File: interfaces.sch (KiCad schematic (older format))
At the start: 69 parts, among them IC3 TPD8S009DSMR, J4 WE_629105150521, J6 685119134923, J7 1140084168, Q2 BSS138APW, Q3 BSS138APW, Q4 BSS138APW, Q5 BSS138APW, Q6 BSS138APW, U12 FT2232HQ

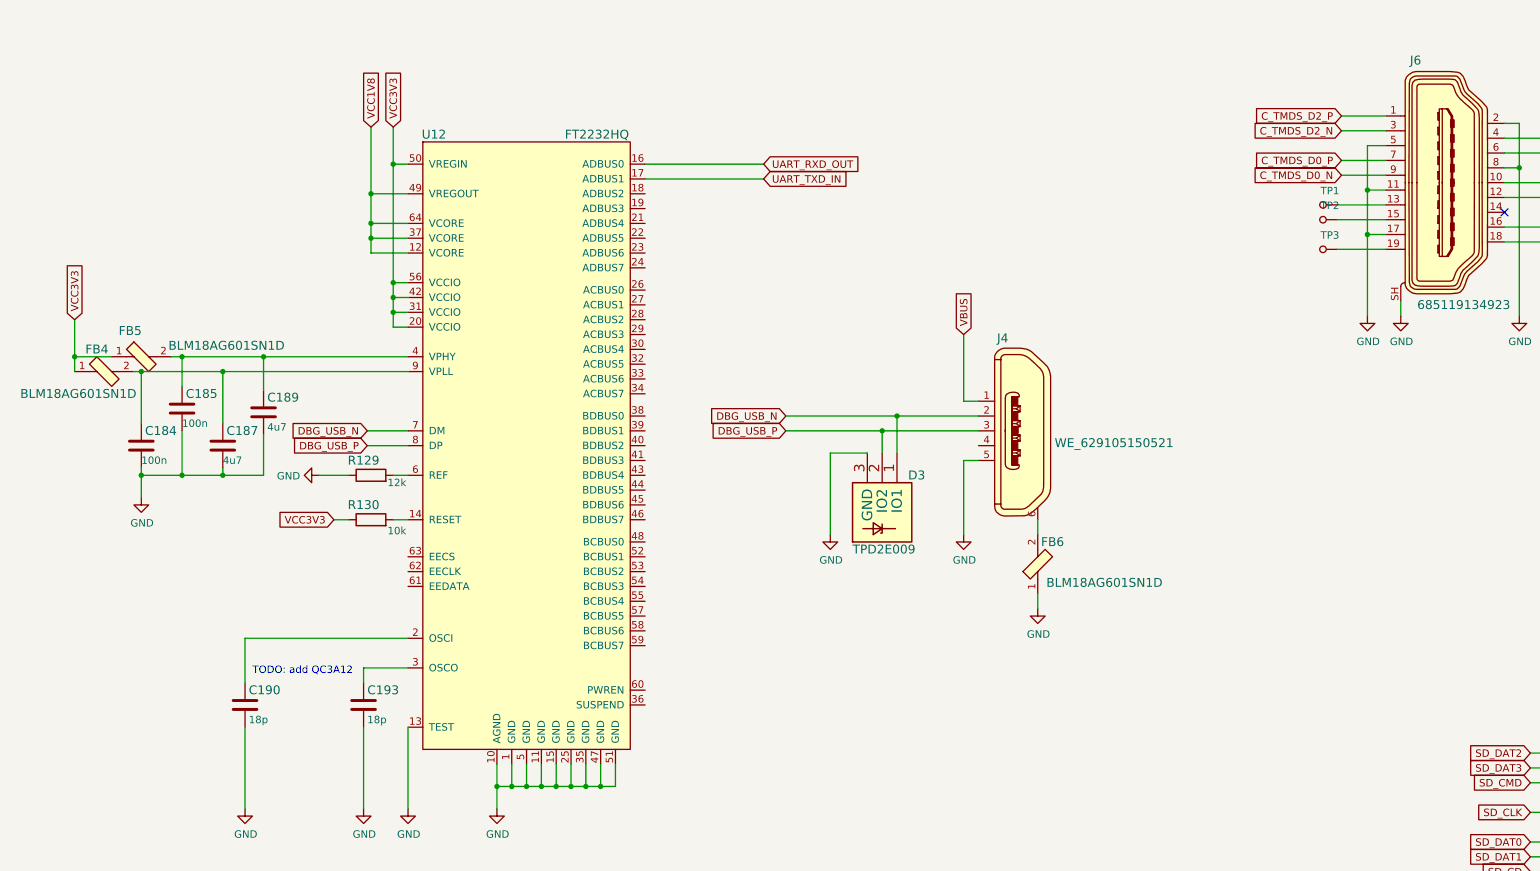
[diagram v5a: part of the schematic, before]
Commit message: Introduce FT4232HQ
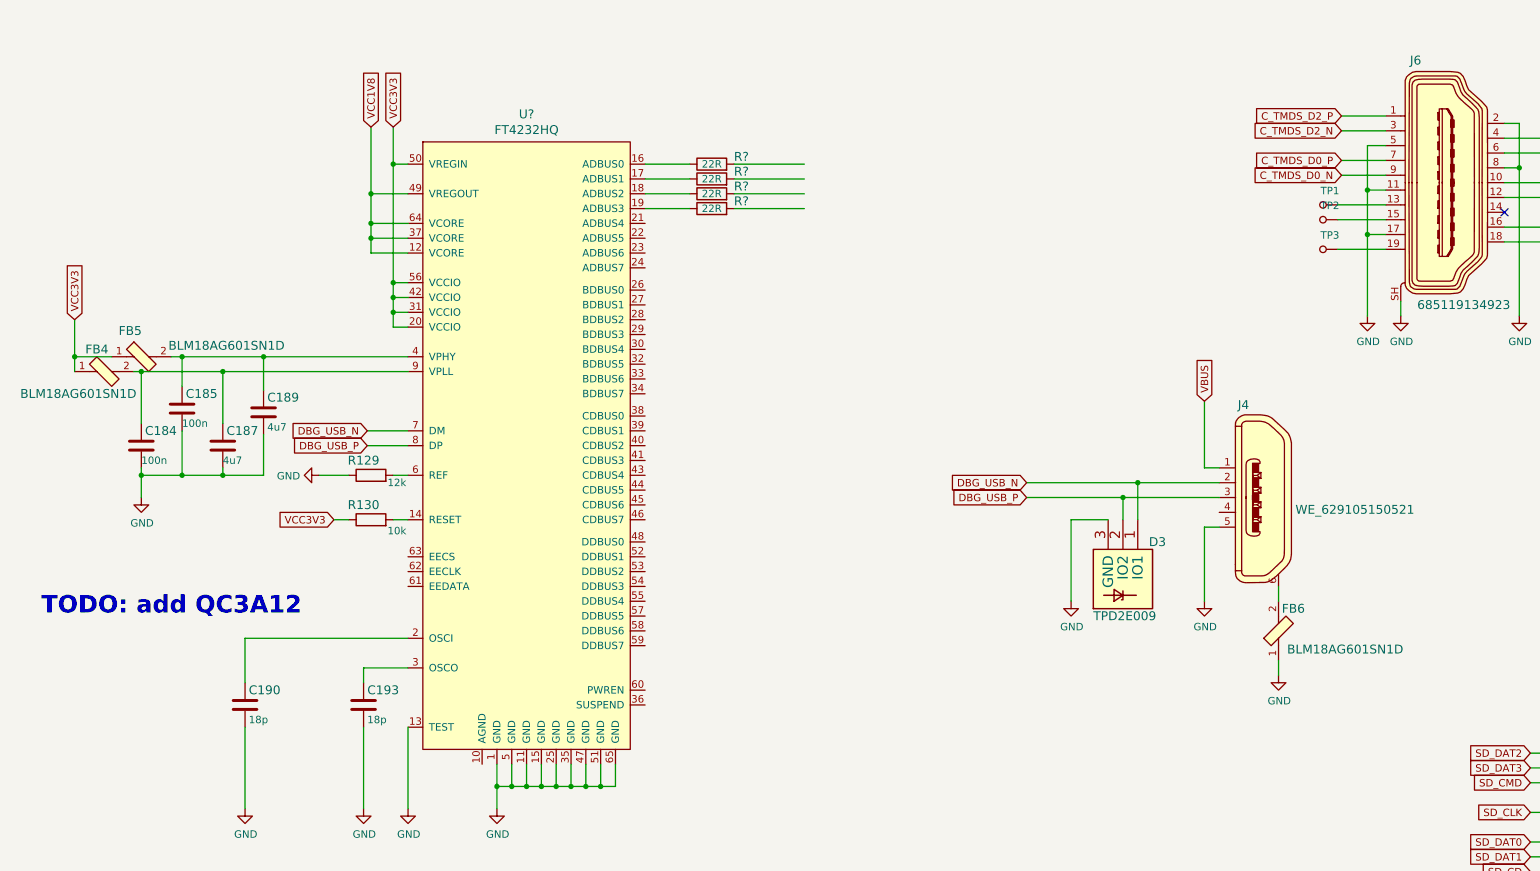
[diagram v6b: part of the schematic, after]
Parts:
- removed U12: FT2232HQ, lpddr4-test-board-footprints:QFN50P900X900X100-65N, symbol lpddr4-test-board:FT2232HQ
- added R? (x4): R_22R_0402, antmicro-footprints:0402-res, symbol antmicroResistors0402:R_22R_0402
- added U?: FT4232HQ, antmicro-footprints:FT4232HQ, symbol antmicroInterfaceControllers:FT4232HQ
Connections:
- net DBG_USB_N: now also U?.7 (DM)
- net DBG_USB_P: now also U?.8 (DP)
- net GND: now also U?.1 (GND), U?.11 (GND), U?.13 (TEST), U?.15 (GND), U?.25 (GND), U?.35 (GND), U?.47 (GND), U?.5 (GND), U?.51 (GND), U?.65 (GND)
- net VCC1V8: now also U?.12 (VCORE), U?.37 (VCORE), U?.49 (VREGOUT), U?.64 (VCORE)
- net VCC3V3: now also U?.20 (VCCIO), U?.31 (VCCIO), U?.42 (VCCIO), U?.50 (VREGIN), U?.56 (VCCIO)
- net at C185.1, C189.1, FB5.2: now also U?.4 (VPHY)
- net at C184.1, C187.1, FB4.2: now also U?.9 (VPLL)
- net at R129.2: now also U?.6 (REF)
- net at R130.2: now also U?.14 (RESET)
- net at C190.1: now also U?.2 (OSCI)
- net at C193.1: now also U?.3 (OSCO)
- new net: R?.1, U?.16 (ADBUS0)
- new net: R?.1, U?.17 (ADBUS1)
- new net: R?.1, U?.18 (ADBUS2)
- new net: R?.1, U?.19 (ADBUS3)
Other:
- moved on the sheet: D3, FB6, J4
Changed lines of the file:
@@
 Comment4 ""
 $EndDescr
-Text GLabel 5950 3000 2    50   Input ~ 0
-UART_RXD_OUT
-Text GLabel 5950 3100 2    50   Input ~ 0
-UART_TXD_IN
-Wire Wire Line
-	5150 3000 5950 3000
-Wire Wire Line
-	5150 3100 5950 3100
 Wire Wire Line
 	3550 3000 3450 3000
@@
 Wire Wire Line
 	3150 5400 3050 5400
-Text Notes 2500 6450 0    50   ~ 0
+Text Notes 1075 6050 0    118  ~ 24
 TODO: add QC3A12
 Wire Wire Line
@@
 	1    0    0    -1
 $EndComp
-$Comp
-L lpddr4-test-board:FT2232HQ U12
-U 1 1 600E77E5
-P 4350 5150
-F 0 "U12" H 3725 7500 60  0000 C CNN
-F 1 "FT2232HQ" H 4825 7500 60  0000 C CNN
-F 2 "lpddr4-test-board-footprints:QFN50P900X900X100-65N" V 4550 5350 60  0001 L CNN
-F 3 "https://www.ftdichip.com/Support/Documents/DataSheets/ICs/DS_FT2232H.pdf" H 4550 5550 60  0001 L CNN
-F 4 "FTDI" H 4550 6300 60  0001 L CNN "Manufacturer"
-F 5 "FT2232HQ-TRAY" H 4550 5700 60  0001 L CNN "MPN"
-	1    4350 5150
-	1    0    0    -1
-$EndComp
 Wire Wire Line
 	4150 7050 4150 7200
@@
 L lpddr4-test-board:WE_629105150521 J4
 U 1 1 60021F87
-P 7700 4800
-F 0 "J4" H 7875 5425 60  0000 R CNN
-F 1 "WE_629105150521" H 7486 4718 60  0000 R CNN
-F 2 "lpddr4-test-board-footprints:USB_Micro_B_Female_629105150521" H 7900 5000 60  0001 L CNN
-F 3 "" H 7900 5100 60  0001 L CNN
-F 4 "629105150521" H 7900 5300 60  0001 L CNN "MPN"
-F 5 "Wurth_Elektronik" H 7900 5900 60  0001 L CNN "Manufacturer"
-	1    7700 4800
+P 9325 5250
+F 0 "J4" H 9500 5875 60  0000 R CNN
+F 1 "WE_629105150521" H 9111 5168 60  0000 R CNN
+F 2 "lpddr4-test-board-footprints:USB_Micro_B_Female_629105150521" H 9525 5450 60  0001 L CNN
+F 3 "" H 9525 5550 60  0001 L CNN
+F 4 "629105150521" H 9525 5750 60  0001 L CNN "MPN"
+F 5 "Wurth_Elektronik" H 9525 6350 60  0001 L CNN "Manufacturer"
+	1    9325 5250
 	-1   0    0    -1
 $EndComp
 Wire Wire Line
-	7400 5000 7300 5000
-Wire Wire Line
-	7300 5000 7300 5500
+	9025 5450 8925 5450
+Wire Wire Line
+	8925 5450 8925 5950
 $Comp
 L lpddr4-test-board:GND #PWR0226
 U 1 1 6002BAB6
-P 7300 5500
-F 0 "#PWR0226" H 7300 5250 50  0001 C CNN
-F 1 "GND" H 7305 5327 50  0000 C CNN
-F 2 "" H 7300 5500 50  0001 C CNN
-F 3 "" H 7300 5500 50  0001 C CNN
-	1    7300 5500
+P 8925 5950
+F 0 "#PWR0226" H 8925 5700 50  0001 C CNN
+F 1 "GND" H 8930 5777 50  0000 C CNN
+F 2 "" H 8925 5950 50  0001 C CNN
+F 3 "" H 8925 5950 50  0001 C CNN
+	1    8925 5950
 	1    0    0    -1
 $EndComp
@@
 L lpddr4-test-board:BLM18AG601SN1D FB6
 U 1 1 6002DC37
-P 7800 5700
-F 0 "FB6" V 7950 5600 60  0000 C CNN
-F 1 "BLM18AG601SN1D" V 7675 5250 60  0000 C CNN
-F 2 "lpddr4-test-board-footprints:0603" H 8000 5900 60  0001 L CNN
-F 3 "https://www.murata.com/en-us/products/productdata/8796738650142/ENFA0003.pdf" H 8000 6000 60  0001 L CNN
-F 4 "BLM18AG601SN1D" H 8000 6200 60  0001 L CNN "MPN"
-F 5 "Murata Electronics North America" H 8000 6800 60  0001 L CNN "Manufacturer"
-	1    7800 5700
+P 9425 6150
+F 0 "FB6" V 9575 6050 60  0000 C CNN
+F 1 "BLM18AG601SN1D" V 9300 5700 60  0000 C CNN
+F 2 "lpddr4-test-board-footprints:0603" H 9625 6350 60  0001 L CNN
+F 3 "https://www.murata.com/en-us/products/productdata/8796738650142/ENFA0003.pdf" H 9625 6450 60  0001 L CNN
+F 4 "BLM18AG601SN1D" H 9625 6650 60  0001 L CNN "MPN"
+F 5 "Murata Electronics North America" H 9625 7250 60  0001 L CNN "Manufacturer"
+	1    9425 6150
 	0    -1   -1   0
 $EndComp
-Text GLabel 6100 4700 0    50   Input ~ 0
+Text GLabel 7725 5150 0    50   Input ~ 0
 DBG_USB_N
-Text GLabel 6100 4800 0    50   Input ~ 0
+Text GLabel 7725 5250 0    50   Input ~ 0
 DBG_USB_P
 Wire Wire Line
-	7400 4600 7300 4600
-Wire Wire Line
-	7300 4600 7300 4150
+	9025 5050 8925 5050
+Wire Wire Line
+	8925 5050 8925 4600
 Text GLabel 2350 8375 1    50   Input ~ 0
 VCC3V3
@@
 L lpddr4-test-board:TPD2E009 D3
 U 1 1 6003C213
-P 6850 5150
-F 0 "D3" V 6800 5225 60  0000 L CNN
-F 1 "TPD2E009" V 7300 4850 60  0000 L CNN
-F 2 "lpddr4-test-board-footprints:SOT-3" H 6900 5350 60  0001 C CNN
-F 3 "https://www.ti.com/lit/ds/symlink/tpd2e009.pdf?ts=1597910439511&ref_url=https%253A%252F%252Fwww.google.com%252F" H 6850 5150 60  0001 C CNN
-F 4 "TPD2E009DRTR" H 6550 5450 50  0001 C CNN "MPN"
-F 5 "Texas Instruments" H 6550 5550 50  0001 C CNN "Manufacturer"
-	1    6850 5150
-	0    1    1    0
-$EndComp
-Wire Wire Line
-	6100 4700 6850 4700
-Wire Wire Line
-	6100 4800 6750 4800
-Wire Wire Line
-	6850 4950 6850 4700
-Connection ~ 6850 4700
-Wire Wire Line
-	6850 4700 7400 4700
-Wire Wire Line
-	6750 4950 6750 4800
-Connection ~ 6750 4800
-Wire Wire Line
-	6750 4800 7400 4800
-Wire Wire Line
-	6650 4950 6400 4950
-Wire Wire Line
-	6400 4950 6400 5500
+P 8475 5600
+F 0 "D3" V 8425 5675 60  0000 L CNN
+F 1 "TPD2E009" V 8925 5300 60  0000 L CNN
+F 2 "lpddr4-test-board-footprints:SOT-3" H 8525 5800 60  0001 C CNN
+F 3 "https://www.ti.com/lit/ds/symlink/tpd2e009.pdf?ts=1597910439511&ref_url=https%253A%252F%252Fwww.google.com%252F" H 8475 5600 60  0001 C CNN
+F 4 "TPD2E009DRTR" H 8175 5900 50  0001 C CNN "MPN"
+F 5 "Texas Instruments" H 8175 6000 50  0001 C CNN "Manufacturer"
+	1    8475 5600
+	0    1    1    0
+$EndComp
+Wire Wire Line
+	7725 5150 8475 5150
+Wire Wire Line
+	7725 5250 8375 5250
+Wire Wire Line
+	8475 5400 8475 5150
+Connection ~ 8475 5150
+Wire Wire Line
+	8475 5150 9025 5150
+Wire Wire Line
+	8375 5400 8375 5250
+Connection ~ 8375 5250
+Wire Wire Line
+	8375 5250 9025 5250
+Wire Wire Line
+	8275 5400 8025 5400
+Wire Wire Line
+	8025 5400 8025 5950
 $Comp
 L lpddr4-test-board:GND #PWR0228
 U 1 1 60049482
-P 6400 5500
-F 0 "#PWR0228" H 6400 5250 50  0001 C CNN
-F 1 "GND" H 6405 5327 50  0000 C CNN
-F 2 "" H 6400 5500 50  0001 C CNN
-F 3 "" H 6400 5500 50  0001 C CNN
-	1    6400 5500
+P 8025 5950
+F 0 "#PWR0228" H 8025 5700 50  0001 C CNN
+F 1 "GND" H 8030 5777 50  0000 C CNN
+F 2 "" H 8025 5950 50  0001 C CNN
+F 3 "" H 8025 5950 50  0001 C CNN
+	1    8025 5950
 	1    0    0    -1
 $EndComp
@@
 Text GLabel 3050 5400 0    50   Input ~ 0
 VCC3V3
-Text GLabel 7300 4150 1    50   Input ~ 0
+Text GLabel 8925 4600 1    50   Input ~ 0
 VBUS
 $Comp
@@
 L lpddr4-test-board:GND #PWR0227
 U 1 1 6002DF17
-P 7800 6000
-F 0 "#PWR0227" H 7800 5750 50  0001 C CNN
-F 1 "GND" H 7805 5827 50  0000 C CNN
-F 2 "" H 7800 6000 50  0001 C CNN
-F 3 "" H 7800 6000 50  0001 C CNN
-	1    7800 6000
+P 9425 6450
+F 0 "#PWR0227" H 9425 6200 50  0001 C CNN
+F 1 "GND" H 9430 6277 50  0000 C CNN
+F 2 "" H 9425 6450 50  0001 C CNN
+F 3 "" H 9425 6450 50  0001 C CNN
+	1    9425 6450
 	1    0    0    -1
 $EndComp
@@
 	11125 7775 11300 7775
 Wire Wire Line
-	7800 5400 7800 5500
-Wire Wire Line
-	7800 5900 7800 6000
+	9425 5850 9425 5950
+Wire Wire Line
+	9425 6350 9425 6450
 $Comp
 L lpddr4-test-board:GND #PWR0167
@@
 Text Notes 4300 8225 0    118  ~ 24
 User buttons
+$Comp
+L antmicroInterfaceControllers:FT4232HQ U?
+U 1 1 601044E5
+P 4350 5150
+F 0 "U?" H 4350 7637 60  0000 C CNN
+F 1 "FT4232HQ" H 4350 7531 60  0000 C CNN
+F 2 "antmicro-footprints:FT4232HQ" V 4550 5350 60  0001 L CNN
+F 3 "https://www.ftdichip.com/Support/Documents/DataSheets/ICs/DS_FT4232H.pdf" H 4550 5550 60  0001 L CNN
+F 4 "FTDI" H 4550 6300 60  0001 L CNN "Manufacturer"
+F 5 "FT4232HQ-TRAY" H 4550 5700 60  0001 L CNN "MPN"
+	1    4350 5150
+	1    0    0    -1
+$EndComp
+$Comp
+L antmicroResistors0402:R_22R_0402 R?
+U 1 1 6013A2FD
+P 5600 3000
+F 0 "R?" H 5800 3050 60  0000 C CNN
+F 1 "R_22R_0402" H 5600 2850 60  0001 C CNN
+F 2 "antmicro-footprints:0402-res" H 5800 3200 60  0001 L CNN
+F 3 "" H 5600 3000 50  0001 C CNN
+F 4 "VISHAY" H 5800 3400 60  0001 L CNN "Manufacturer"
+F 5 "CRCW040222R0FKED" H 5800 3300 60  0001 L CNN "MPN"
+F 6 "22R" H 5600 3000 50  0000 C CNN "Val"
+	1    5600 3000
+	1    0    0    -1
+$EndComp
+$Comp
+L antmicroResistors0402:R_22R_0402 R?
+U 1 1 6013A700
+P 5600 3100
+F 0 "R?" H 5800 3150 60  0000 C CNN
+F 1 "R_22R_0402" H 5600 2950 60  0001 C CNN
+F 2 "antmicro-footprints:0402-res" H 5800 3300 60  0001 L CNN
+F 3 "" H 5600 3100 50  0001 C CNN
+F 4 "VISHAY" H 5800 3500 60  0001 L CNN "Manufacturer"
+F 5 "CRCW040222R0FKED" H 5800 3400 60  0001 L CNN "MPN"
+F 6 "22R" H 5600 3100 50  0000 C CNN "Val"
+	1    5600 3100
+	1    0    0    -1
+$EndComp
+$Comp
+L antmicroResistors0402:R_22R_0402 R?
+U 1 1 6013A969
+P 5600 3200
+F 0 "R?" H 5800 3250 60  0000 C CNN
+F 1 "R_22R_0402" H 5600 3050 60  0001 C CNN
+F 2 "antmicro-footprints:0402-res" H 5800 3400 60  0001 L CNN
+F 3 "" H 5600 3200 50  0001 C CNN
+F 4 "VISHAY" H 5800 3600 60  0001 L CNN "Manufacturer"
+F 5 "CRCW040222R0FKED" H 5800 3500 60  0001 L CNN "MPN"
+F 6 "22R" H 5600 3200 50  0000 C CNN "Val"
+	1    5600 3200
+	1    0    0    -1
+$EndComp
+$Comp
+L antmicroResistors0402:R_22R_0402 R?
+U 1 1 6013AB72
+P 5600 3300
+F 0 "R?" H 5800 3350 60  0000 C CNN
+F 1 "R_22R_0402" H 5600 3150 60  0001 C CNN
+F 2 "antmicro-footprints:0402-res" H 5800 3500 60  0001 L CNN
+F 3 "" H 5600 3300 50  0001 C CNN
+F 4 "VISHAY" H 5800 3700 60  0001 L CNN "Manufacturer"
+F 5 "CRCW040222R0FKED" H 5800 3600 60  0001 L CNN "MPN"
+F 6 "22R" H 5600 3300 50  0000 C CNN "Val"
+	1    5600 3300
+	1    0    0    -1
+$EndComp
+Wire Wire Line
+	5450 3000 5150 3000
+Wire Wire Line
+	5150 3100 5450 3100
+Wire Wire Line
+	5450 3200 5150 3200
+Wire Wire Line
+	5150 3300 5450 3300
+Wire Wire Line
+	5750 3000 6225 3000
+Wire Wire Line
+	5750 3100 6225 3100
+Wire Wire Line
+	5750 3200 6225 3200
+Wire Wire Line
+	5750 3300 6225 3300
 $EndSCHEMATC

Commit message: Route FTDI filtering
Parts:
- added U8: SRST, symbol antmicroTestPoints:test
- gave numbers to parts that had none: 5
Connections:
- net at U7.22 (ADBUS5): now also U8.1
- net TCK_JTAG: now reaches R18.2
- net TDI_JTAG: now reaches R19.2
- net TDO_JTAG: now reaches R20.2
- net TMS_JTAG: now reaches R25.2
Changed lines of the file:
@@
 User buttons
 $Comp
-L antmicroInterfaceControllers:FT4232HQ U?
+L antmicroInterfaceControllers:FT4232HQ U7
 U 1 1 601044E5
 P 4350 5150
-F 0 "U?" H 4350 7637 60  0000 C CNN
+F 0 "U7" H 4350 7637 60  0000 C CNN
 F 1 "FT4232HQ" H 4350 7531 60  0000 C CNN
 F 2 "antmicro-footprints:FT4232HQ" V 4550 5350 60  0001 L CNN
@@
 $EndComp
 $Comp
-L antmicroResistors0402:R_22R_0402 R?
+L antmicroResistors0402:R_22R_0402 R18
 U 1 1 6013A2FD
 P 5600 3000
-F 0 "R?" H 5800 3050 60  0000 C CNN
+F 0 "R18" H 5800 3050 60  0000 C CNN
 F 1 "R_22R_0402" H 5600 2850 60  0001 C CNN
 F 2 "antmicro-footprints:0402-res" H 5800 3200 60  0001 L CNN
@@
 $EndComp
 $Comp
-L antmicroResistors0402:R_22R_0402 R?
+L antmicroResistors0402:R_22R_0402 R19
 U 1 1 6013A700
 P 5600 3100
-F 0 "R?" H 5800 3150 60  0000 C CNN
+F 0 "R19" H 5800 3150 60  0000 C CNN
 F 1 "R_22R_0402" H 5600 2950 60  0001 C CNN
 F 2 "antmicro-footprints:0402-res" H 5800 3300 60  0001 L CNN
@@
 $EndComp
 $Comp
-L antmicroResistors0402:R_22R_0402 R?
+L antmicroResistors0402:R_22R_0402 R20
 U 1 1 6013A969
 P 5600 3200
-F 0 "R?" H 5800 3250 60  0000 C CNN
+F 0 "R20" H 5800 3250 60  0000 C CNN
 F 1 "R_22R_0402" H 5600 3050 60  0001 C CNN
 F 2 "antmicro-footprints:0402-res" H 5800 3400 60  0001 L CNN
@@
 $EndComp
 $Comp
-L antmicroResistors0402:R_22R_0402 R?
+L antmicroResistors0402:R_22R_0402 R25
 U 1 1 6013AB72
 P 5600 3300
-F 0 "R?" H 5800 3350 60  0000 C CNN
+F 0 "R25" H 5800 3350 60  0000 C CNN
 F 1 "R_22R_0402" H 5600 3150 60  0001 C CNN
 F 2 "antmicro-footprints:0402-res" H 5800 3500 60  0001 L CNN
@@
 Wire Wire Line
 	5750 3300 6225 3300
+Text GLabel 6225 3000 2    50   Input ~ 0
+TCK_JTAG
+Text GLabel 6225 3100 2    50   Input ~ 0
+TDI_JTAG
+Text GLabel 6225 3200 2    50   Input ~ 0
+TDO_JTAG
+Text GLabel 6225 3300 2    50   Input ~ 0
+TMS_JTAG
+Wire Wire Line
+	5150 3500 5500 3500
+$Comp
+L antmicroTestPoints:test U8
+U 1 1 601E16F4
+P 5700 3450
+F 0 "U8" V 5631 3500 50  0000 R CNN
+F 1 "SRST" V 5586 3500 50  0001 R CNN
+F 2 "" H 5700 3450 50  0001 C CNN
+F 3 "" H 5700 3450 50  0001 C CNN
+	1    5700 3450
+	0    -1   -1   0
+$EndComp
 $EndSCHEMATC

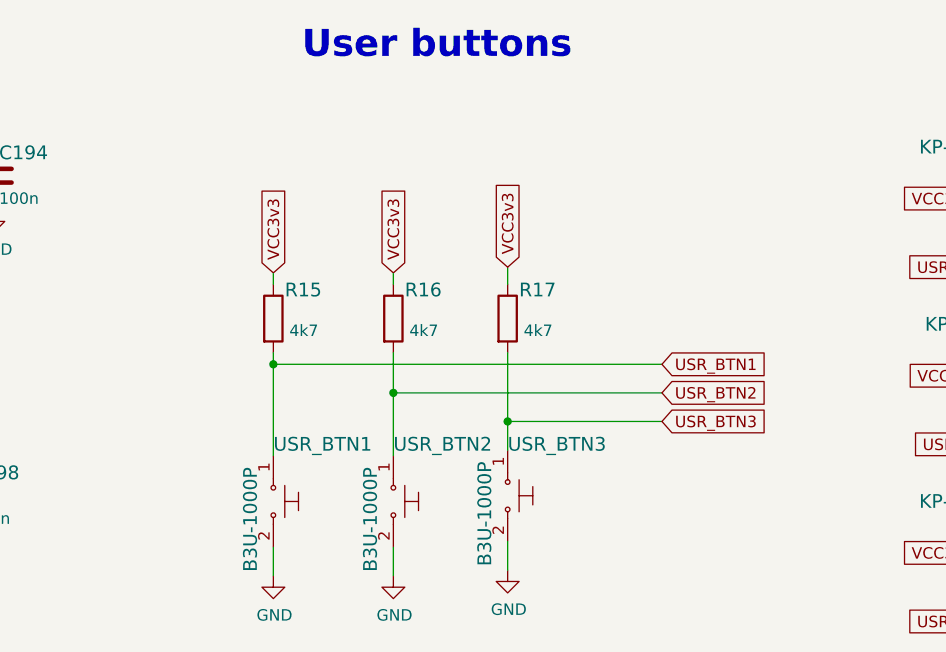
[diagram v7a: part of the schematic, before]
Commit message: Update buttons and LEDs connection
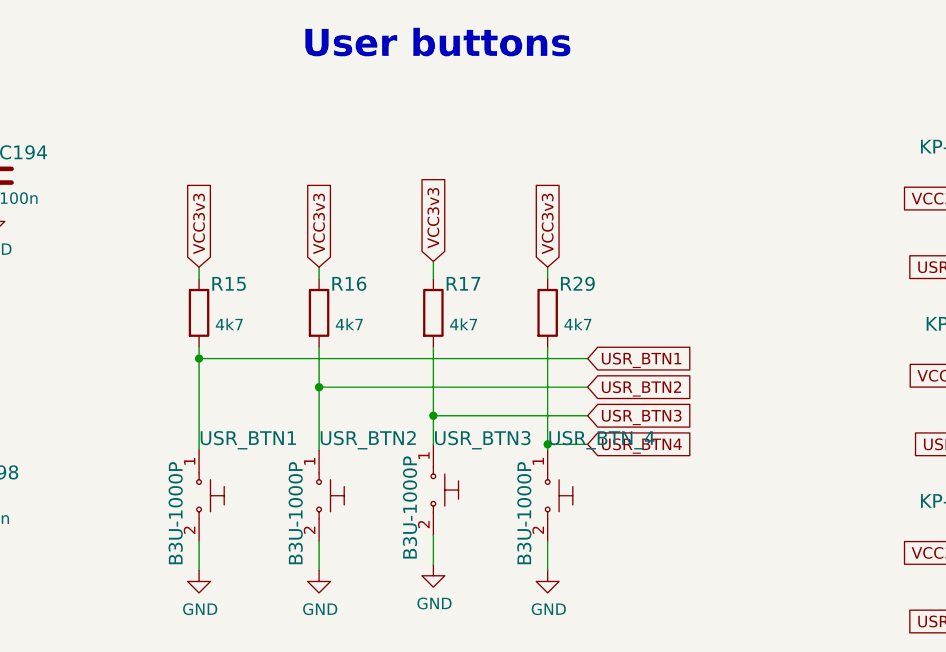
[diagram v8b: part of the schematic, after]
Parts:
- added R29: R_4k7_0402, lpddr4-test-board-footprints:0402-res, symbol lpddr4-test-board:R_4k7_0402
- added USR_BTN_4: B3U-1000P, lpddr4-test-board-footprints:Switch_Tactile_SMD_B3U-1000P, symbol lpddr4-test-board:B3U-1000P
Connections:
- net GND: now also USR_BTN_4.2
- net VCC3v3: now also R29.1
- new net USR_BTN4: R29.2, USR_BTN_4.1
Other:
- moved on the sheet: R15, R16, R17, USR_BTN1, USR_BTN2, USR_BTN3
